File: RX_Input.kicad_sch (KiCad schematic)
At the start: 1 part, among them J1 PCB.SMAFRA.HT

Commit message: More filter work. Add project title to drawings.
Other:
- company: (none) -> Steves Custom Computers
- title: (none) -> PLUTO RF Card Front-End
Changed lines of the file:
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@@
 (kicad_sch (version 20230121) (generator eeschema)
   (paper "A4")
+  (title_block
+    (title "PLUTO RF Card Front-End")
+    (rev " 001")
+    (company "Steves Custom Computers")
+  )
   (junction (at 63.5 34.29) (diameter 0) (color 0 0 0 0)
   )

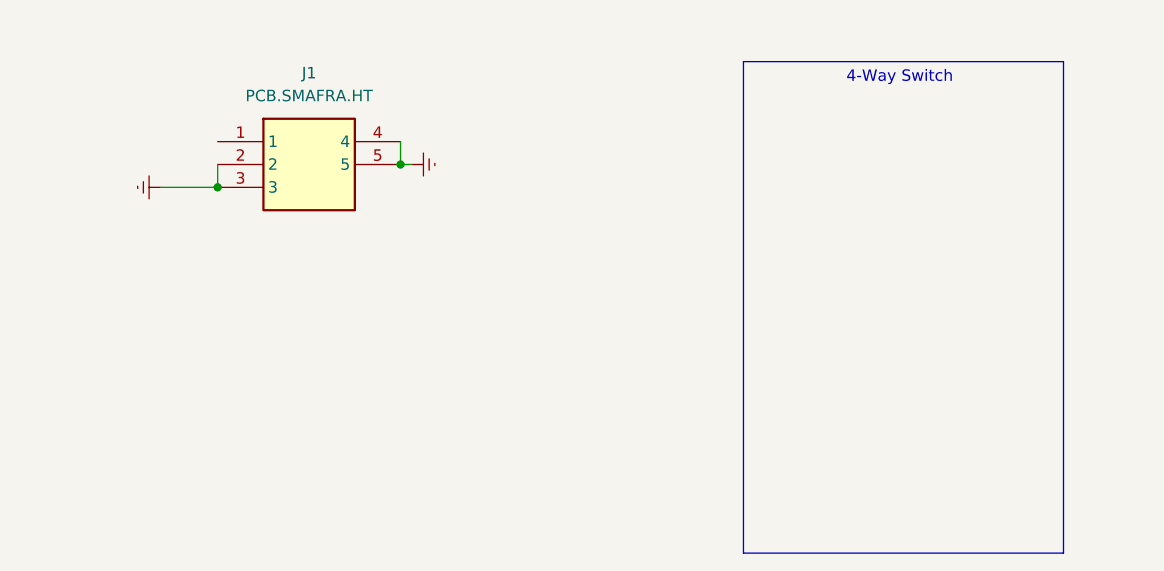
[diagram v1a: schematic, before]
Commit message: Major restructure. Add power/control busses.
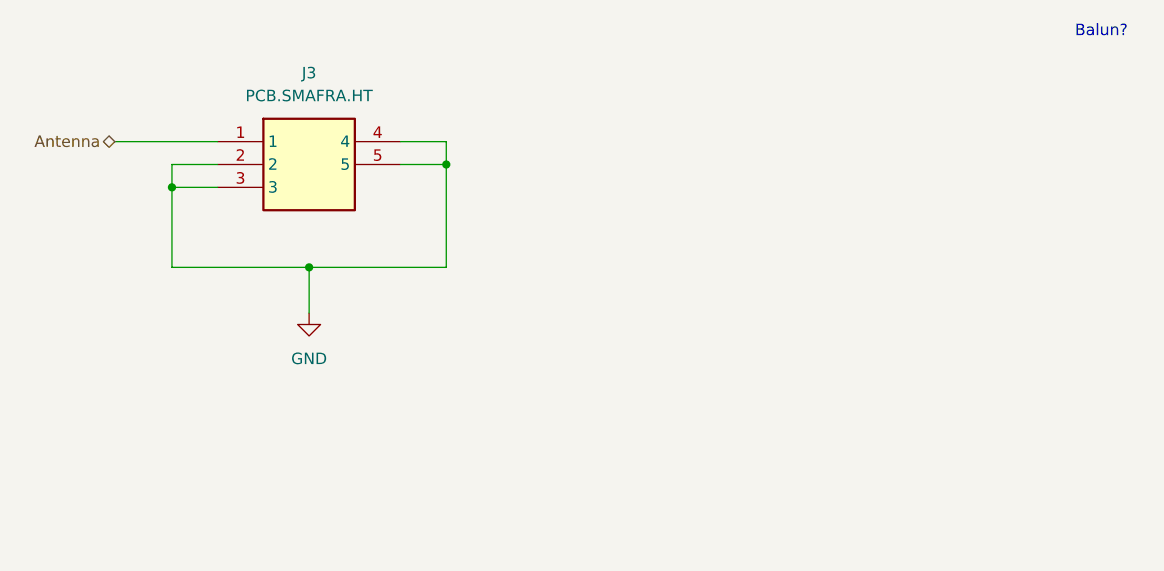
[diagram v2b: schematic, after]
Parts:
- removed J1: PCB.SMAFRA.HT, SamacSys_Parts:PCBSMAFRAHT, symbol SamacSys_Parts:PCB.SMAFRA.HT
- added J3: PCB.SMAFRA.HT, PCBSMAFRAHT, symbol Mouser:PCB.SMAFRA.HT
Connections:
- new net Antenna: J3.1
- new net GND: J3.2, J3.3, J3.4, J3.5
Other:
- note added: "Balun?"
- note removed: "4-Way Switch"
- title: PLUTO RF Card Front-End -> PLUTO RF Front-End Card
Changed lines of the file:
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@@
   (paper "A4")
   (title_block
-    (title "PLUTO RF Card Front-End")
+    (title "PLUTO RF Front-End Card")
     (rev " 001")
     (company "Steves Custom Computers")
   )
-  (junction (at 63.5 34.29) (diameter 0) (color 0 0 0 0)
+  (junction (at 38.1 36.83) (diameter 0) (color 0 0 0 0)
   )
-  (junction (at 43.18 36.83) (diameter 0) (color 0 0 0 0)
+  (junction (at 68.58 34.29) (diameter 0) (color 0 0 0 0)
   )
-  (wire (pts (xy 63.5 31.75) (xy 63.5 34.29))
+  (junction (at 53.34 45.72) (diameter 0) (color 0 0 0 0)
+  )
+  (wire (pts (xy 68.58 34.29) (xy 68.58 45.72))
     (stroke (width 0) (type default))
   )
-  (wire (pts (xy 43.18 34.29) (xy 43.18 36.83))
+  (wire (pts (xy 38.1 45.72) (xy 38.1 36.83))
     (stroke (width 0) (type default))
   )
-  (wire (pts (xy 36.83 36.83) (xy 43.18 36.83))
+  (wire (pts (xy 68.58 31.75) (xy 68.58 34.29))
     (stroke (width 0) (type default))
   )
-  (wire (pts (xy 63.5 34.29) (xy 64.77 34.29))
+  (wire (pts (xy 31.75 31.75) (xy 43.18 31.75))
     (stroke (width 0) (type default))
   )
-  (rectangle (start 101.6 22.86) (end 137.16 77.47)
+  (wire (pts (xy 38.1 45.72) (xy 53.34 45.72))
     (stroke (width 0) (type default))
-    (fill (type none))
   )
-  (text "4-Way Switch" (at 113.03 25.4 0)
+  (wire (pts (xy 38.1 34.29) (xy 43.18 34.29))
+    (stroke (width 0) (type default))
+  )
+  (wire (pts (xy 53.34 45.72) (xy 68.58 45.72))
+    (stroke (width 0) (type default))
+  )
+  (wire (pts (xy 53.34 50.8) (xy 53.34 45.72))
+    (stroke (width 0) (type default))
+  )
+  (wire (pts (xy 38.1 36.83) (xy 43.18 36.83))
+    (stroke (width 0) (type default))
+  )
+  (wire (pts (xy 63.5 31.75) (xy 68.58 31.75))
+    (stroke (width 0) (type default))
+  )
+  (wire (pts (xy 63.5 34.29) (xy 68.58 34.29))
+    (stroke (width 0) (type default))
+  )
+  (wire (pts (xy 38.1 36.83) (xy 38.1 34.29))
+    (stroke (width 0) (type default))
+  )
+  (text "Balun?" (at 138.43 20.32 0)
     (effects (font (size 1.27 1.27)) (justify left bottom))
   )
-  (symbol (lib_id "SamacSys_Parts:PCB.SMAFRA.HT") (at 43.18 31.75 0) (unit 1)
+  (hierarchical_label "Antenna" (shape bidirectional) (at 31.75 31.75 180) (fields_autoplaced)
+    (effects (font (size 1.27 1.27)) (justify right))
+  )
+  (symbol (lib_id "Mouser:PCB.SMAFRA.HT") (at 43.18 31.75 0) (unit 1)
     (in_bom yes) (on_board yes) (dnp no) (fields_autoplaced)
-    (property "Reference" "J1" (at 53.34 24.13 0)
+    (property "Reference" "J3" (at 53.34 24.13 0)
       (effects (font (size 1.27 1.27)))
     )
@@
       (effects (font (size 1.27 1.27)))
     )
-    (property "Footprint" "SamacSys_Parts:PCBSMAFRAHT" (at 59.69 126.67 0)
+    (property "Footprint" "PCBSMAFRAHT" (at 59.69 126.67 0)
       (effects (font (size 1.27 1.27)) (justify left top) hide)
     )
-    (property "Datasheet" "https://www.mouser.com/datasheet/2/398/PCB_SMAFRA_HT-3137267.pdf" (at 59.69 226.67 0)
+    (property "Datasheet" "" (at 59.69 226.67 0)
       (effects (font (size 1.27 1.27)) (justify left top) hide)
     )
@@
     (instances
       (project "UpDownConverter"
-        (path "/cc9fcf9b-b84f-49ca-8b98-f0ff7034b4a0"
-          (reference "J1") (unit 1)
-        )
-        (path "/cc9fcf9b-b84f-49ca-8b98-f0ff7034b4a0/32631ea7-57a7-4016-8f88-d0d0383e4511"
-          (reference "J1") (unit 1)
-        )
         (path "/cc9fcf9b-b84f-49ca-8b98-f0ff7034b4a0/c51ecb37-5de8-4a39-8f06-f77413a33545"
-          (reference "J1") (unit 1)
+          (reference "J3") (unit 1)
         )
       )
     )
   )
-  (symbol (lib_id "power:Earth") (at 36.83 36.83 270) (unit 1)
-    (in_bom yes) (on_board yes) (dnp no)
-    (property "Reference" "#PWR01" (at 30.48 36.83 0)
+  (symbol (lib_id "power:GND") (at 53.34 50.8 0) (unit 1)
+    (in_bom yes) (on_board yes) (dnp no) (fields_autoplaced)
+    (property "Reference" "#PWR01" (at 53.34 57.15 0)
       (effects (font (size 1.27 1.27)) hide)
     )
-    (property "Value" "Earth" (at 33.02 36.83 0)
+    (property "Value" "GND" (at 53.34 55.88 0)
+      (effects (font (size 1.27 1.27)))
+    )
+    (property "Footprint" "" (at 53.34 50.8 0)
       (effects (font (size 1.27 1.27)) hide)
     )
-    (property "Footprint" "" (at 36.83 36.83 0)
-      (effects (font (size 1.27 1.27)) hide)
-    )
-    (property "Datasheet" "~" (at 36.83 36.83 0)
+    (property "Datasheet" "" (at 53.34 50.8 0)
       (effects (font (size 1.27 1.27)) hide)
     )
@@
     (instances
       (project "UpDownConverter"
-        (path "/cc9fcf9b-b84f-49ca-8b98-f0ff7034b4a0"
-          (reference "#PWR01") (unit 1)
-        )
-        (path "/cc9fcf9b-b84f-49ca-8b98-f0ff7034b4a0/32631ea7-57a7-4016-8f88-d0d0383e4511"
-          (reference "#PWR01") (unit 1)
-        )
         (path "/cc9fcf9b-b84f-49ca-8b98-f0ff7034b4a0/c51ecb37-5de8-4a39-8f06-f77413a33545"
           (reference "#PWR01") (unit 1)
         )
       )
-    )
-  )
-  (symbol (lib_id "power:Earth") (at 64.77 34.29 90) (unit 1)
-    (in_bom yes) (on_board yes) (dnp no) (fields_autoplaced)
-    (property "Reference" "#PWR02" (at 71.12 34.29 0)
-      (effects (font (size 1.27 1.27)) hide)
-    )
-    (property "Value" "Earth" (at 68.58 34.29 0)
-      (effects (font (size 1.27 1.27)) hide)
-    )
-    (property "Footprint" "" (at 64.77 34.29 0)
-      (effects (font (size 1.27 1.27)) hide)
-    )
-    (property "Datasheet" "~" (at 64.77 34.29 0)
-      (effects (font (size 1.27 1.27)) hide)
-    )
-    (pin "1")
-    (instances
-      (project "UpDownConverter"
-        (path "/cc9fcf9b-b84f-49ca-8b98-f0ff7034b4a0"
-          (reference "#PWR02") (unit 1)
-        )
-        (path "/cc9fcf9b-b84f-49ca-8b98-f0ff7034b4a0/32631ea7-57a7-4016-8f88-d0d0383e4511"
-          (reference "#PWR02") (unit 1)
-        )
-        (path "/cc9fcf9b-b84f-49ca-8b98-f0ff7034b4a0/c51ecb37-5de8-4a39-8f06-f77413a33545"
-          (reference "#PWR02") (unit 1)
-        )
-      )
